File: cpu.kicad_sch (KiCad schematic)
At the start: 15 parts, among them IC19 MC6809E, SW1 RESET

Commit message: work on memory sub system
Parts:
- R1, R13, R14, R36, R40, R41: footprint Resistor_THT:R_Axial_DIN0309_L9.0mm_D3.2mm_P12.70mm_Horizontal -> Dragon:R_Axial_DIN0309_L9.0mm_D2.5mm_P12.70mm_Horizontal
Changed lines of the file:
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@@
 			)
 		)
-		(property "Footprint" "Resistor_THT:R_Axial_DIN0309_L9.0mm_D3.2mm_P12.70mm_Horizontal"
+		(property "Footprint" "Dragon:R_Axial_DIN0309_L9.0mm_D2.5mm_P12.70mm_Horizontal"
 			(at 28.702 91.44 90)
 			(effects
@@
 			)
 		)
-		(property "Footprint" "Resistor_THT:R_Axial_DIN0309_L9.0mm_D3.2mm_P12.70mm_Horizontal"
+		(property "Footprint" "Dragon:R_Axial_DIN0309_L9.0mm_D2.5mm_P12.70mm_Horizontal"
 			(at 165.1 105.41 0)
 			(effects
@@
 			)
 		)
-		(property "Footprint" "Resistor_THT:R_Axial_DIN0309_L9.0mm_D3.2mm_P12.70mm_Horizontal"
+		(property "Footprint" "Dragon:R_Axial_DIN0309_L9.0mm_D2.5mm_P12.70mm_Horizontal"
 			(at 57.912 91.44 90)
 			(effects
@@
 			)
 		)
-		(property "Footprint" "Resistor_THT:R_Axial_DIN0309_L9.0mm_D3.2mm_P12.70mm_Horizontal"
+		(property "Footprint" "Dragon:R_Axial_DIN0309_L9.0mm_D2.5mm_P12.70mm_Horizontal"
 			(at 172.085 99.441 0)
 			(effects
@@
 			)
 		)
-		(property "Footprint" "Resistor_THT:R_Axial_DIN0309_L9.0mm_D3.2mm_P12.70mm_Horizontal"
+		(property "Footprint" "Dragon:R_Axial_DIN0309_L9.0mm_D2.5mm_P12.70mm_Horizontal"
 			(at 165.1 99.441 0)
 			(effects
@@
 			)
 		)
-		(property "Footprint" "Resistor_THT:R_Axial_DIN0309_L9.0mm_D3.2mm_P12.70mm_Horizontal"
+		(property "Footprint" "Dragon:R_Axial_DIN0309_L9.0mm_D2.5mm_P12.70mm_Horizontal"
 			(at 178.943 99.441 0)
 			(effects

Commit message: add PIA and VDG to schematics
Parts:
- removed C1: 0.1uF, Capacitor_THT:C_Disc_D4.3mm_W1.9mm_P5.00mm, symbol Device:C_Small
- removed R1: 100K, Dragon:R_Axial_DIN0309_L9.0mm_D2.5mm_P12.70mm_Horizontal, symbol Device:R

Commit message: video circuit tracing
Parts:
- added C23: 100uF, Capacitor_THT:CP_Radial_D8.0mm_P5.00mm, symbol Device:C_Polarized_Small
- added D10, D11, D12: 1N914, Diode_THT:D_DO-35_SOD27_P12.70mm_Horizontal, symbol Diode:1N914
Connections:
- net +5V: now also D12.1 (K)
- net A7: now also D10.2 (A)
- net GND: now also C23.2
- net ~{HALT}: now also D11.2 (A)
- net ~{RES}: now also D10.1 (K)
- new net: C23.1, D11.1 (K), D12.2 (A)

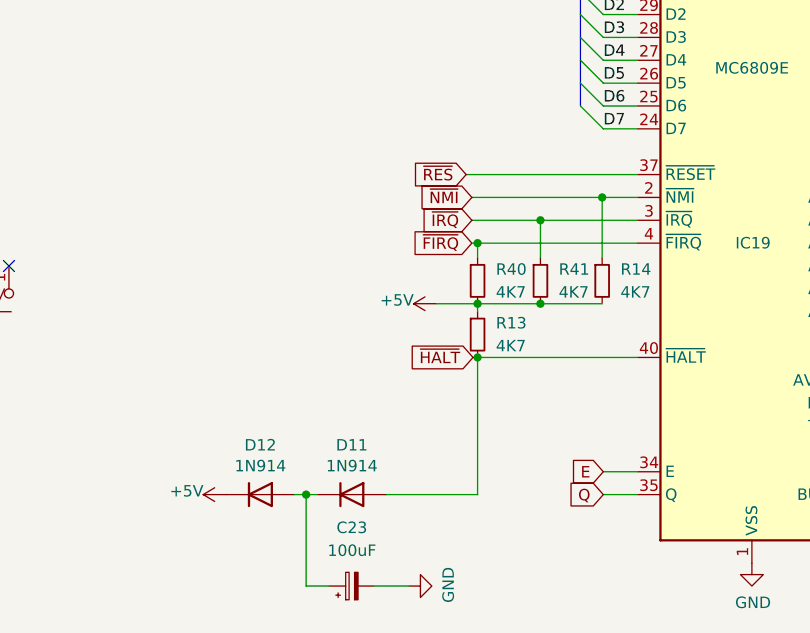
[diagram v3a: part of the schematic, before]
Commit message: FM generator routing
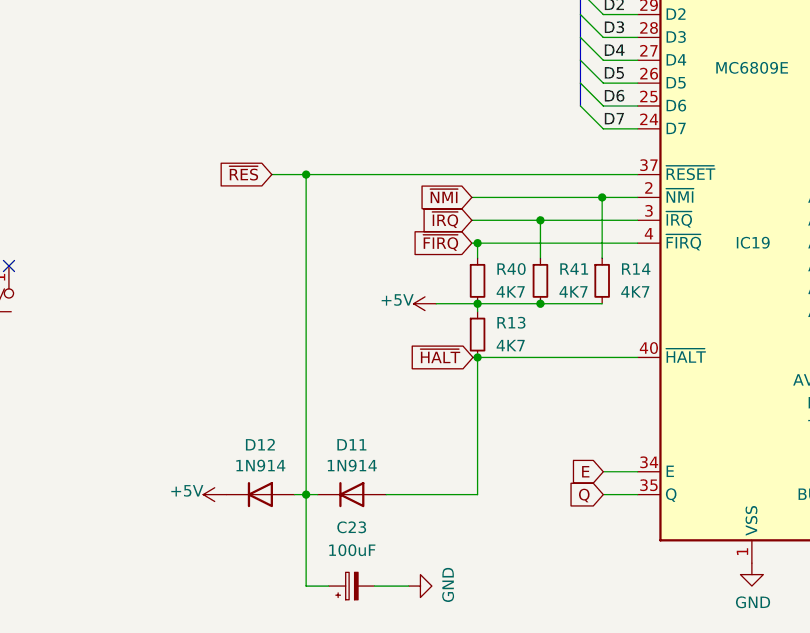
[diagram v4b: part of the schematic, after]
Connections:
- net ~{RES}: now also C23.1, D11.1 (K), D12.2 (A)
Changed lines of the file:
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@@
+	)
+	(junction
+		(at 146.05 87.63)
+		(diameter 0)
+		(color 0 0 0 0)
 	)
 	(junction
@@
 	(wire
 		(pts
+			(xy 146.05 123.19) (xy 146.05 87.63)
+		)
+		(stroke
+			(width 0)
+			(type default)
+		)
+	)
+	(wire
+		(pts
 			(xy 203.2 49.53) (xy 205.74 49.53)
 		)
@@
 	(wire
 		(pts
-			(xy 163.83 87.63) (xy 182.88 87.63)
+			(xy 142.24 87.63) (xy 146.05 87.63)
 		)
 		(stroke
@@
 		(pts
 			(xy 176.53 77.47) (xy 176.53 80.01)
+		)
+		(stroke
+			(width 0)
+			(type default)
+		)
+	)
+	(wire
+		(pts
+			(xy 146.05 87.63) (xy 182.88 87.63)
 		)
 		(stroke
@@
 	(global_label "~{RES}"
 		(shape input)
-		(at 163.83 87.63 180)
+		(at 142.24 87.63 180)
 		(fields_autoplaced yes)
 		(effects
@@
 		)
 		(property "Intersheetrefs" "${INTERSHEET_REFS}"
-			(at 157.2163 87.63 0)
+			(at 135.6263 87.63 0)
 			(effects
 				(font

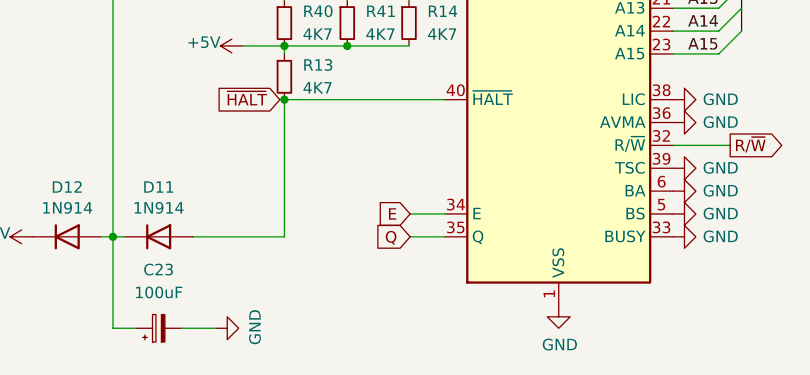
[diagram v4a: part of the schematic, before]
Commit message: complete physical layout
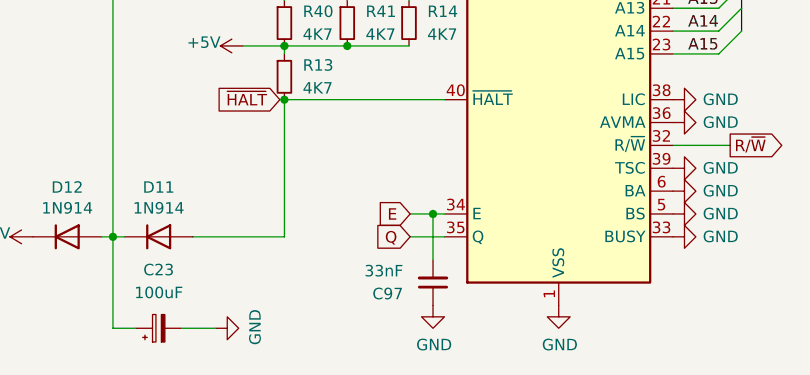
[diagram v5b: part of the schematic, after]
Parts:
- added C97: 33nF, Capacitor_THT:C_Disc_D3.0mm_W2.0mm_P2.50mm, symbol Device:C_Small
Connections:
- net E: now also C97.2
- net GND: now also C97.1
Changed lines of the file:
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@@
+	)
+	(junction
+		(at 181.61 120.65)
+		(diameter 0)
+		(color 0 0 0 0)
 	)
 	(junction
@@
 		)
 	)
+	(wire
+		(pts
+			(xy 181.61 125.73) (xy 181.61 120.65)
+		)
+		(stroke
+			(width 0)
+			(type default)
+		)
+	)
 	(bus
 		(pts
@@
 	(wire
 		(pts
-			(xy 179.07 120.65) (xy 182.88 120.65)
+			(xy 179.07 120.65) (xy 181.61 120.65)
 		)
 		(stroke
@@
 		(pts
 			(xy 215.9 64.77) (xy 215.9 67.31)
+		)
+		(stroke
+			(width 0)
+			(type default)
+		)
+	)
+	(wire
+		(pts
+			(xy 181.61 120.65) (xy 182.88 120.65)
 		)
 		(stroke
@@
 	(symbol
 		(lib_id "power:GND")
+		(at 181.61 130.81 0)
+		(unit 1)
+		(exclude_from_sim no)
+		(in_bom yes)
+		(on_board yes)
+		(dnp no)
+		(property "Reference" "#PWR0191"
+			(at 181.61 137.16 0)
+			(effects
+				(font
+					(size 1.27 1.27)
+				)
+				(hide yes)
+			)
+		)
+		(property "Value" "GND"
+			(at 181.737 135.2042 0)
+			(effects
+				(font
+					(size 1.27 1.27)
+				)
+			)
+		)
+		(property "Footprint" ""
+			(at 181.61 130.81 0)
+			(effects
+				(font
+					(size 1.27 1.27)
+				)
+				(hide yes)
+			)
+		)
+		(property "Datasheet" ""
+			(at 181.61 130.81 0)
+			(effects
+				(font
+					(size 1.27 1.27)
+				)
+				(hide yes)
+			)
+		)
+		(property "Description" ""
+			(at 181.61 130.81 0)
+			(effects
+				(font
+					(size 1.27 1.27)
+				)
+				(hide yes)
+			)
+		)
+		(pin "1"
+		)
+		(instances
+			(project "Dragon32Issue2ASecam"
+				(path "/e3d9e4a2-26cb-4482-98c1-138d9a22d1eb/1b81cb51-a21c-47a6-a425-f1e0ecc2ba52"
+					(reference "#PWR0191")
+					(unit 1)
+				)
+			)
+		)
+	)
+	(symbol
+		(lib_id "power:GND")
 		(at 208.28 120.65 90)
 		(unit 1)
@@
 					(unit 1)
 				)
+			)
+		)
+	)
+	(symbol
+		(lib_id "Device:C_Small")
+		(at 181.61 128.27 180)
+		(unit 1)
+		(exclude_from_sim no)
+		(in_bom yes)
+		(on_board yes)
+		(dnp no)
+		(property "Reference" "C97"
+			(at 178.308 129.5338 0)
+			(effects
+				(font
+					(size 1.27 1.27)
+				)
+				(justify left)
+			)
+		)
+		(property "Value" "33nF"
+			(at 178.308 126.9938 0)
+			(effects
+				(font
+					(size 1.27 1.27)
+				)
+				(justify left)
+			)
+		)
+		(property "Footprint" "Capacitor_THT:C_Disc_D3.0mm_W2.0mm_P2.50mm"
+			(at 181.61 128.27 0)
+			(effects
+				(font
+					(size 1.27 1.27)
+				)
+				(hide yes)
+			)
+		)
+		(property "Datasheet" "https://www.vishay.com/docs/45171/kseries.pdf"
+			(at 181.61 128.27 0)
+			(effects
+				(font
+					(size 1.27 1.27)
+				)
+				(hide yes)
+			)
+		)
+		(property "Description" ""
+			(at 181.61 128.27 0)
+			(effects
+				(font
+					(size 1.27 1.27)
+				)
+				(hide yes)
+			)
+		)
+		(property "DigiKey" "BC1016CT-ND"
+			(at 181.61 128.27 0)
+			(effects
+				(font
+					(size 1.27 1.27)
+				)
+				(hide yes)
+			)
+		)
+		(pin "1"
+		)
+		(pin "2"
+		)
+		(instances
+			(project "Dragon32Issue2ASecam"
+				(path "/e3d9e4a2-26cb-4482-98c1-138d9a22d1eb/1b81cb51-a21c-47a6-a425-f1e0ecc2ba52"
+					(reference "C97")
+					(unit 1)
+				)
